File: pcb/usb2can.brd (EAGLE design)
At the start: 59 x 15.8 mm, 49 parts, among them CON1 USB_A_MALESMD, IC1 ADM3053M, IC2 LD1117S33

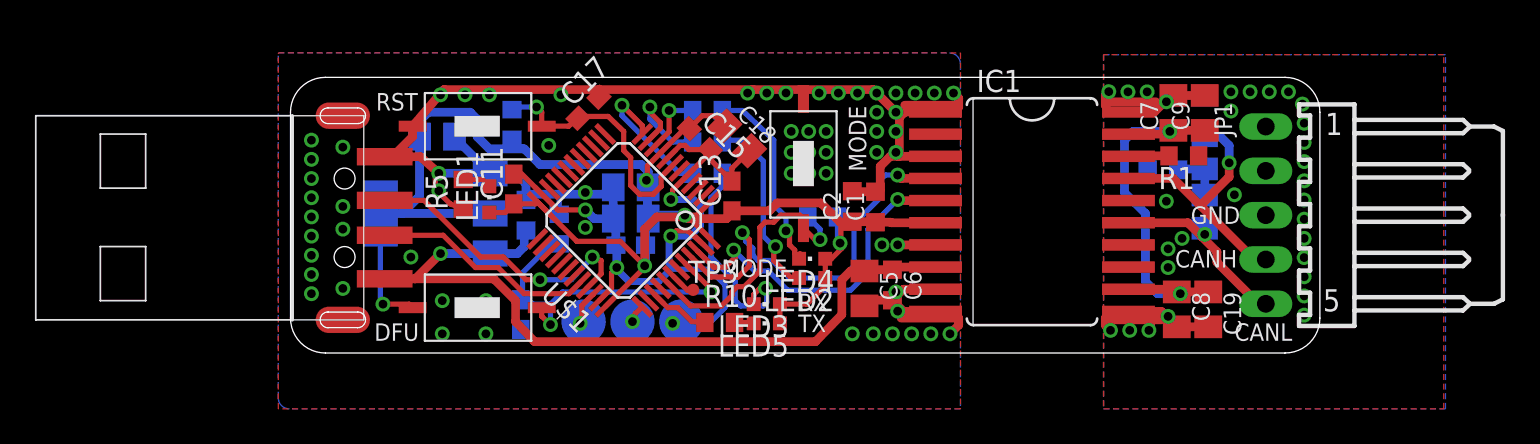
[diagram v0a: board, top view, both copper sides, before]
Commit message: pcb: add bottom pads for USB connector
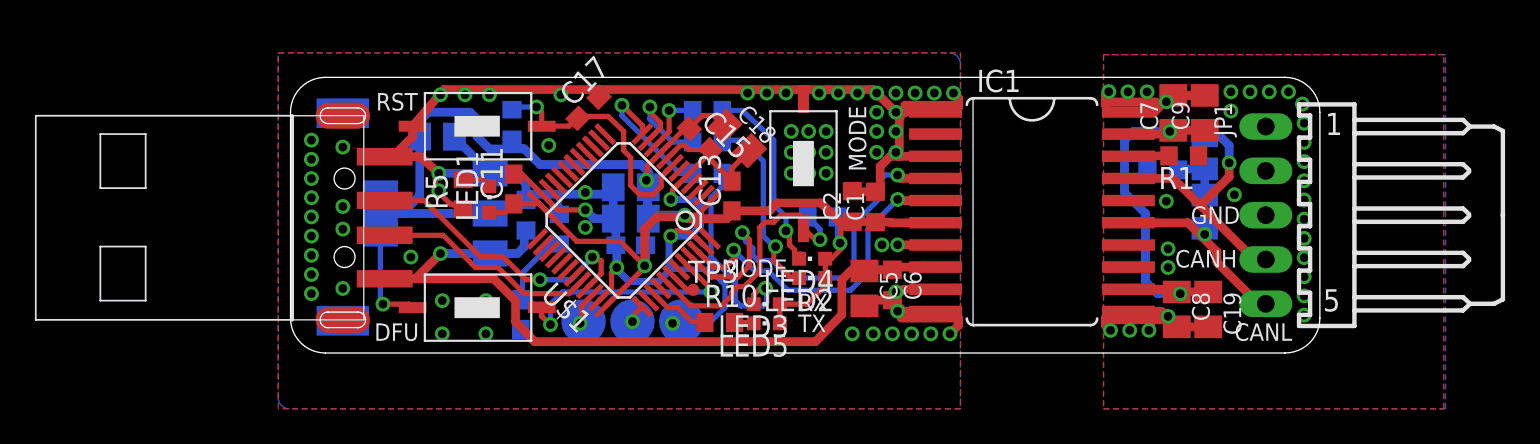
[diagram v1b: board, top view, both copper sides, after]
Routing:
- net GNDA: vias 30 -> 29
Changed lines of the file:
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@@
 <text x="54.1" y="0.7" size="1" layer="59" ratio="16">CANL</text>
 <text x="51.6" y="7.4" size="1" layer="59" ratio="16">GND</text>
+<rectangle x1="1.5" y1="12.9" x2="4.5" y2="14.6" layer="16"/>
+<rectangle x1="1.5" y1="1" x2="4.5" y2="2.7" layer="16"/>
+<rectangle x1="1.5" y1="1" x2="4.5" y2="2.7" layer="30"/>
+<rectangle x1="1.5" y1="12.9" x2="4.5" y2="14.6" layer="30"/>
 </plain>
 <attributes>
@@
 </class>
 </classes>
-<designrules name="LaenPCBOrder *">
+<designrules name="OSHPARK">
 <description language="de">&lt;b&gt;EAGLE Design Rules&lt;/b&gt;
 &lt;p&gt;
@@
 besondere Anforderungen haben, treffen Sie die erforderlichen
 Einstellungen hier und speichern die Design Rules unter
-einem neuen Namen ab.</description>
+einem neuen Namen ab.
+&lt;h1&gt;OSH Park&lt;/h1&gt;</description>
 <description language="en">&lt;b&gt;Laen's PCB Order Design Rules&lt;/b&gt;
 &lt;p&gt;
@@
 <param name="mlMinCreamFrame" value="0mil"/>
 <param name="mlMaxCreamFrame" value="0mil"/>
-<param name="mlViaStopLimit" value="9999mil"/>
+<param name="mlViaStopLimit" value="0mil"/>
 <param name="srRoundness" value="0"/>
 <param name="srMinRoundness" value="0mil"/>
@@
 <wire x1="46.7" y1="2" x2="46.8" y2="1.9" width="0.5" layer="1"/>
 <wire x1="46.8" y1="1.9" x2="49.9" y2="1.9" width="0.5" layer="1"/>
-<via x="51.1" y="6.57" extent="1-16" drill="0.5"/>
 </signal>
 <signal name="N$1">

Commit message: schematic: rename unnamed wires to CANH and CANL.
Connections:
- net N$2 renamed CANL
- net N$3 renamed CANH
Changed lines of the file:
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@@
 <wire x1="48.0542" y1="11.3" x2="50.35" y2="11.3" width="0.5" layer="1"/>
 </signal>
-<signal name="N$2">
+<signal name="CANL">
 <contactref element="IC1" pad="15"/>
 <contactref element="R2" pad="2"/>
@@
 <wire x1="52.4" y1="7.15" x2="52.4" y2="6.8" width="0.5" layer="16"/>
 </signal>
-<signal name="N$3">
+<signal name="CANH">
 <contactref element="IC1" pad="17"/>
 <contactref element="R3" pad="2"/>

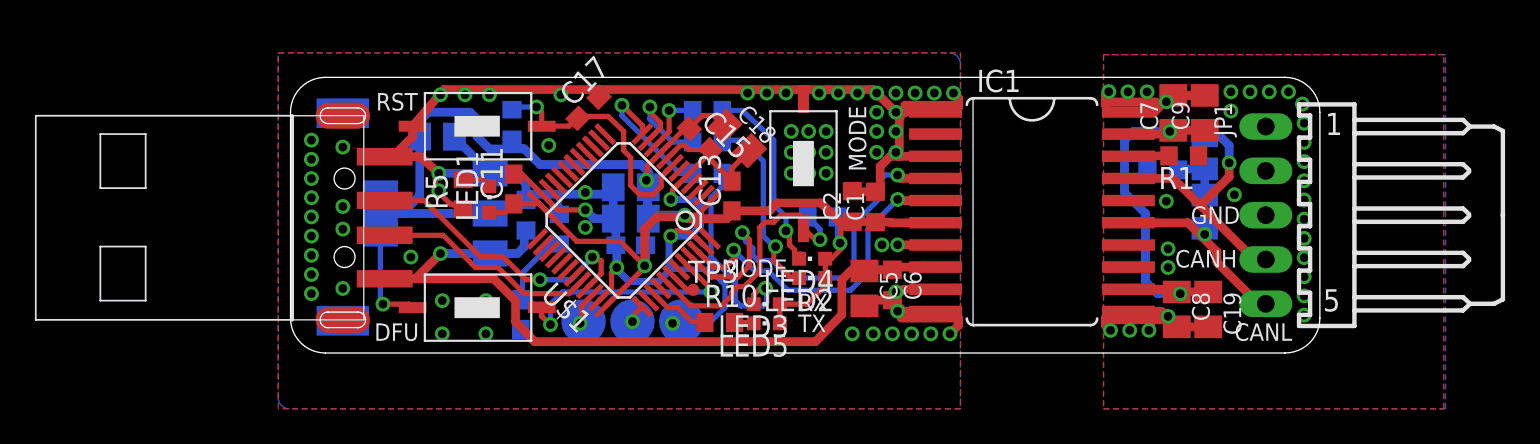
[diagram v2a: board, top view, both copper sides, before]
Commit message: schematic: Bypass Capacitors and Silk Screen
- Bypass capacitors: nearest capacitor should be the smallest.
- Add label to 100n capacitors
- Add label to LEDs
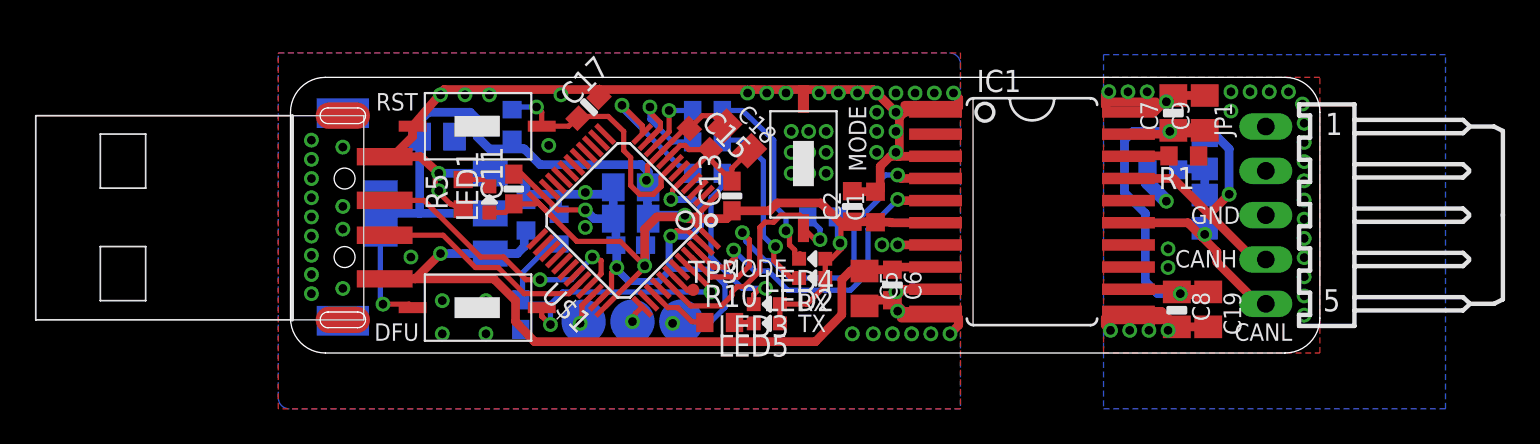
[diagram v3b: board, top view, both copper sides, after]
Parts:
- C19, C9: value 100n -> 10u
- C7: value 10n -> 100n
- C8: value 10u -> 100n
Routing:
- net GND: track 129.8 -> 126.9 mm
- net GNDA: track 18.3 -> 20.6 mm, vias 29 -> 28
- net N$12: track 12.4 -> 10.3 mm
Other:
- board text added: "HW: Daniel"
- board text removed: "HW: Daniel SW: Kevin"
